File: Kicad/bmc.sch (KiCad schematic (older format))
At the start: 26 parts, among them J1601 Header, J1602 Header, J1603 Conn_01x05, J1605 Double-mini-DIN-6, SW1601 SW_DIP_x01, SW1602 SW_DIP_x01, U1601 STM32F031K6T6

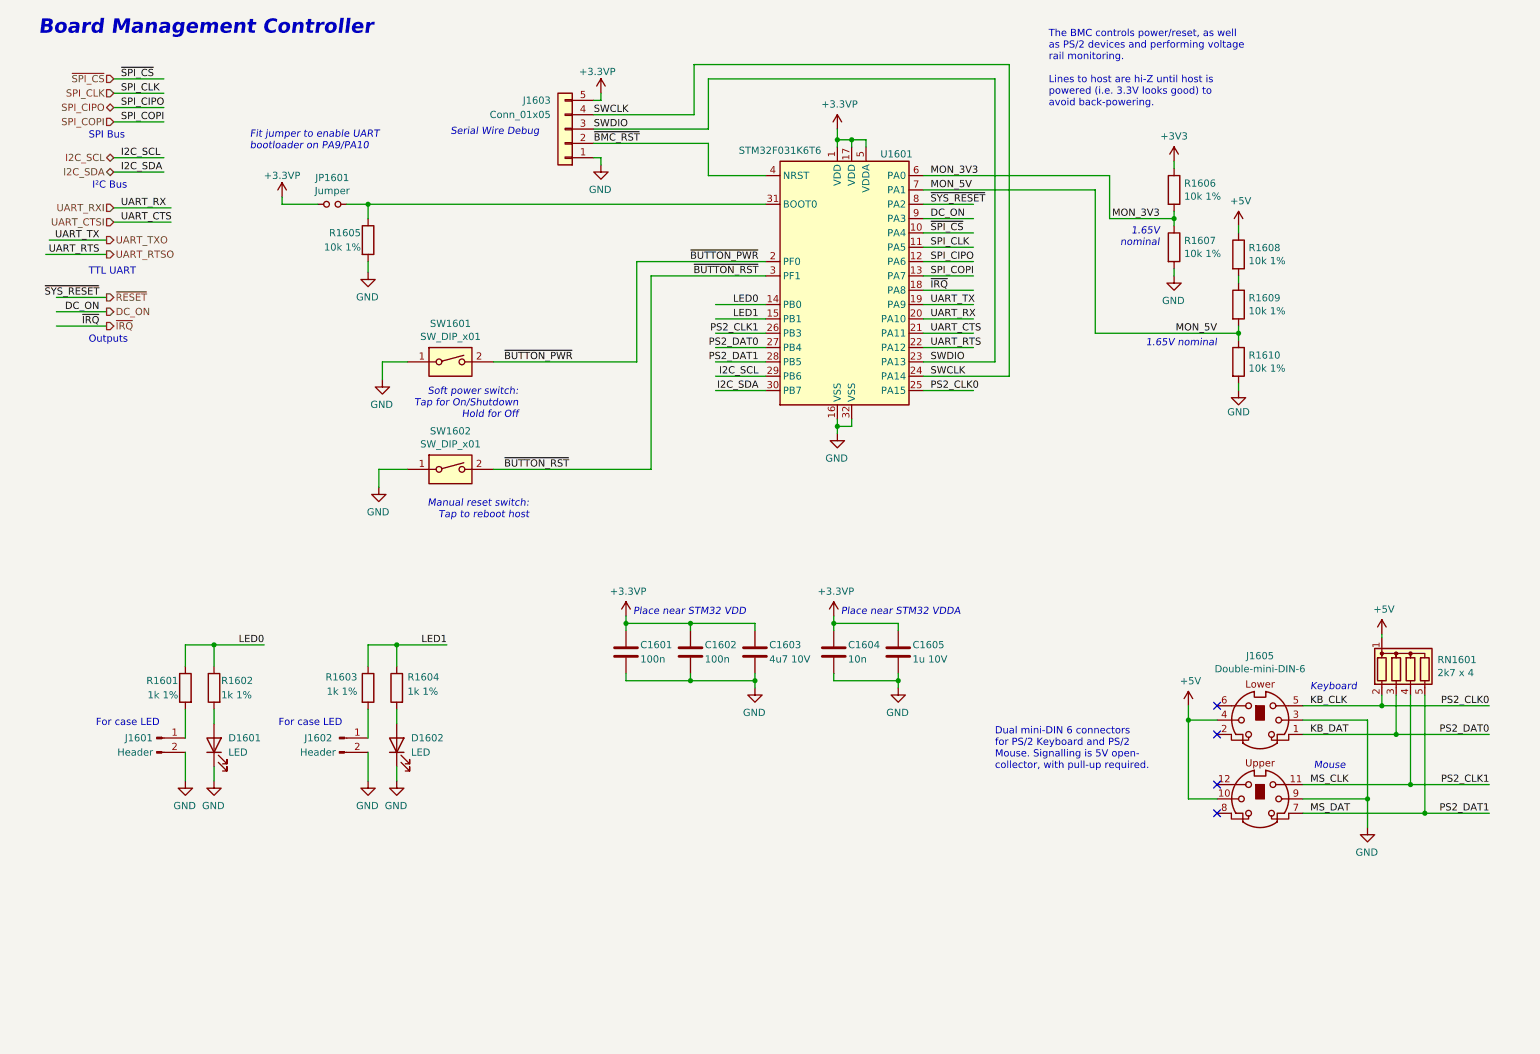
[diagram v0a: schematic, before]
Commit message: Revised PSU switch-on circuit.
Updated notes on BMC and Audio sheet.
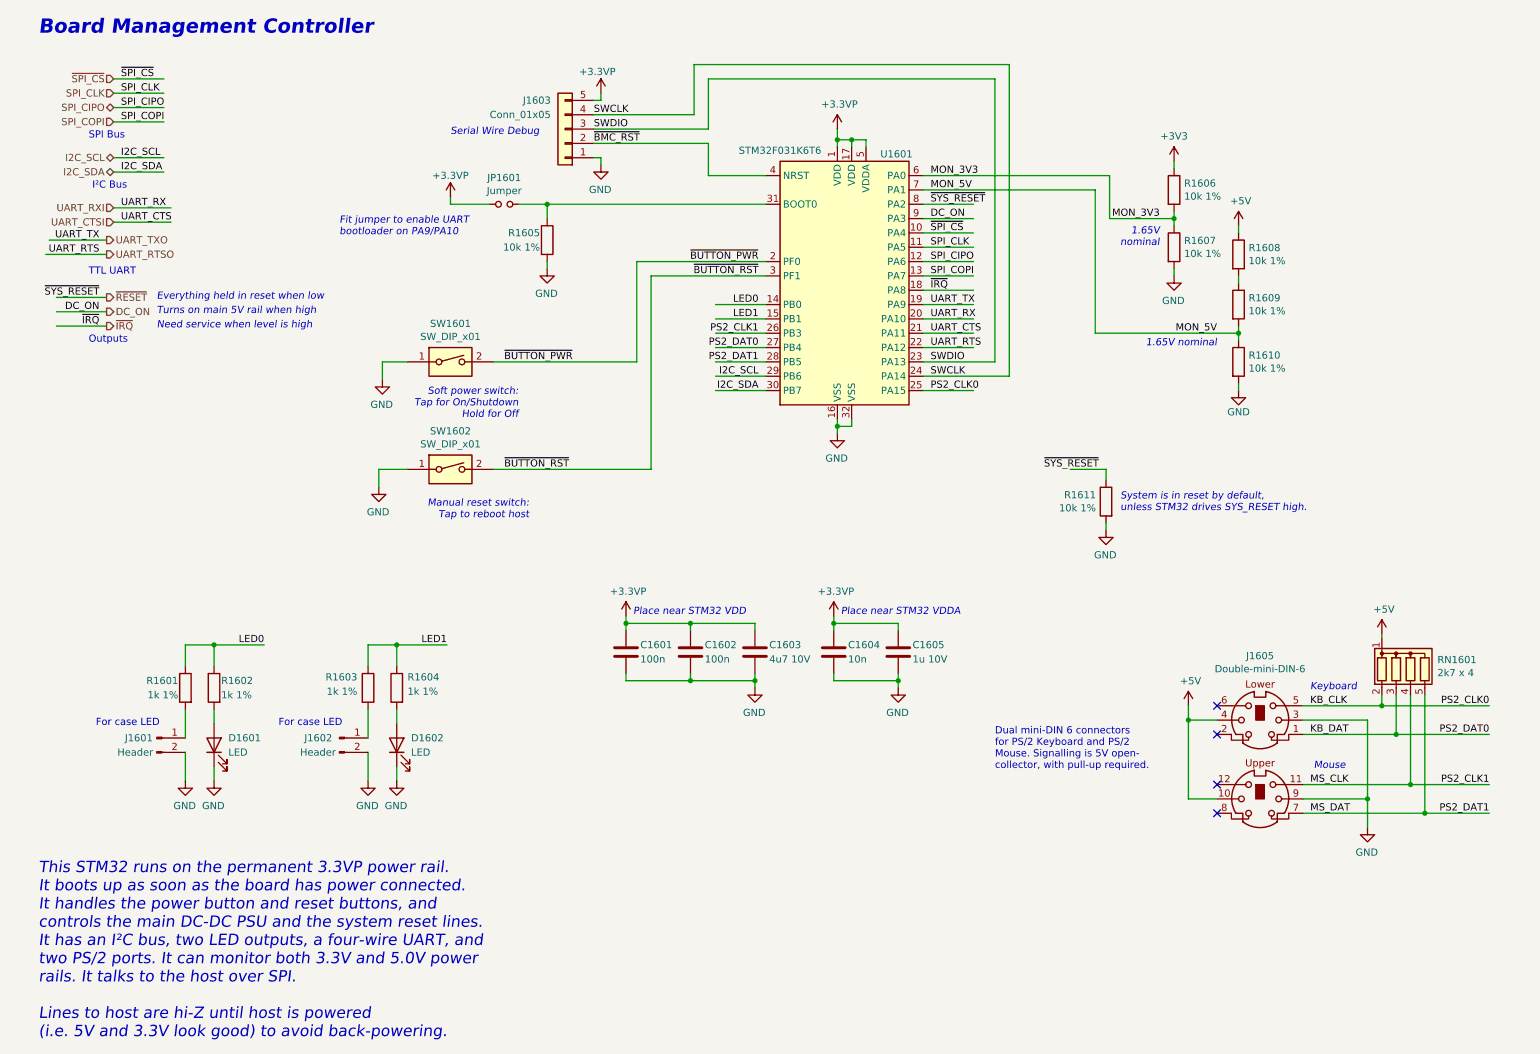
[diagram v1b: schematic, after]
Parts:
- added R1611: 10k 1%, Resistor_SMD:R_0805_2012Metric_Pad1.20x1.40mm_HandSolder, symbol Device:R
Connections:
- wire segments 147 -> 150
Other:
- note added: "Everything held in reset when low"
- note added: "Need service when level is high"
- note added: "System is in reset by default,\nunless STM32 drives SYS_RESET high."
- note added: "This STM32 runs on the permanent 3.3VP power rail.\nIt boots up as soon as the board has power connected.\nIt handles the power button and reset buttons, and\ncontrols the main DC-DC PSU and the system reset lines.\nIt has an I²C bus, two LED outputs, a four-wire UART, and\ntwo PS/2 ports. It can monitor both 3.3V and 5.0V power\nrails. It talks to the host over SPI.\n\nLines to host are hi-Z unt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"
- note added: "Turns on main 5V rail when high"
- note removed: "The BMC controls power/reset, as well\nas PS/2 devices and performing voltage\nrail monitoring.\n\nLines to host are hi-Z until host is\npowered (i.e. 3.3V looks good) to\navoid back-powering."
- moved on the sheet: JP1601, R1605
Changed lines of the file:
@@
 encoding utf-8
 Sheet 16 17
-Title ""
+Title "Neotron Common Hardware - Board M'gmt Controller"
 Date ""
-Rev ""
-Comp ""
-Comment1 ""
-Comment2 ""
+Rev "[Uncontrolled]"
+Comp "https://neotron-compute.github.io/"
+Comment1 "Licenced as CC BY-SA"
+Comment2 "Copyright (c) The Neotron Developers, 2021"
 Comment3 ""
 Comment4 ""
@@
 Text Notes 3975 4075 2    50   Italic 0
 Manual reset switch:\nTap to reboot host
-Text Notes 7600 1200 0    50   ~ 0
-The BMC controls power/reset, as well\nas PS/2 devices and performing voltage\nrail monitoring.\n\nLines to host are hi-Z until host is\npowered (i.e. 3.3V looks good) to\navoid back-powering.
 $Comp
 L Device:C C1603
@@
 L Device:Jumper_NO_Small JP1601
 U 1 1 6072F924
-P 2600 1875
-F 0 "JP1601" H 2600 2060 50  0000 C CNN
-F 1 "Jumper" H 2600 1969 50  0000 C CNN
-F 2 "Connector_PinHeader_2.54mm:PinHeader_1x02_P2.54mm_Vertical" H 2600 1875 50  0001 C CNN
-F 3 "~" H 2600 1875 50  0001 C CNN
-F 4 "1" H 2600 1875 50  0001 C CNN "DNP"
-F 5 "~" H 2600 1875 50  0001 C CNN "Digikey"
-F 6 "~" H 2600 1875 50  0001 C CNN "MPN"
-F 7 "~" H 2600 1875 50  0001 C CNN "Manufacturer"
-	1    2600 1875
+P 3800 1875
+F 0 "JP1601" H 3800 2060 50  0000 C CNN
+F 1 "Jumper" H 3800 1969 50  0000 C CNN
+F 2 "Connector_PinHeader_2.54mm:PinHeader_1x02_P2.54mm_Vertical" H 3800 1875 50  0001 C CNN
+F 3 "~" H 3800 1875 50  0001 C CNN
+F 4 "1" H 3800 1875 50  0001 C CNN "DNP"
+F 5 "~" H 3800 1875 50  0001 C CNN "Digikey"
+F 6 "~" H 3800 1875 50  0001 C CNN "MPN"
+F 7 "~" H 3800 1875 50  0001 C CNN "Manufacturer"
+	1    3800 1875
 	1    0    0    -1
 $EndComp
@@
 L power:+3.3VP #PWR01607
 U 1 1 606E2A06
-P 2250 1825
-F 0 "#PWR01607" H 2400 1775 50  0001 C CNN
-F 1 "+3.3VP" H 2250 1975 50  0000 C CNN
-F 2 "" H 2250 1825 50  0001 C CNN
-F 3 "" H 2250 1825 50  0001 C CNN
-	1    2250 1825
+P 3425 1825
+F 0 "#PWR01607" H 3575 1775 50  0001 C CNN
+F 1 "+3.3VP" H 3425 1975 50  0000 C CNN
+F 2 "" H 3425 1825 50  0001 C CNN
+F 3 "" H 3425 1825 50  0001 C CNN
+	1    3425 1825
 	1    0    0    -1
 $EndComp
@@
 	6325 1425 6325 1475
 Wire Wire Line
-	2250 1825 2250 1875
+	3425 1825 3425 1875
 Wire Wire Line
 	5625 2575 5275 2575
@@
 Serial Wire Debug
 Wire Wire Line
-	2700 1875 2850 1875
+	3900 1875 4100 1875
 Wire Wire Line
 	6725 2975 7225 2975
@@
 MON_3V3
 Wire Wire Line
-	2250 1875 2500 1875
+	3425 1875 3700 1875
 Wire Wire Line
 	9925 5375 10675 5375
@@
 Wire Wire Line
 	6725 2675 7075 2675
-Text Notes 2025 1500 0    50   Italic 0
+Text Notes 2650 2100 0    50   Italic 0
 Fit jumper to enable UART\nbootloader on PA9/PA10
 Wire Wire Line
@@
 L Device:R R1605
 U 1 1 606E29F2
-P 2850 2125
-F 0 "R1605" H 2800 2175 50  0000 R CNN
-F 1 "10k 1%" H 2800 2075 50  0000 R CNN
-F 2 "Resistor_SMD:R_0805_2012Metric_Pad1.20x1.40mm_HandSolder" V 2780 2125 50  0001 C CNN
-F 3 "~" H 2850 2125 50  0001 C CNN
-F 4 "0" H 2850 2125 50  0001 C CNN "DNP"
-F 5 "RMCF0805FT10K0-ND" H 2850 2125 50  0001 C CNN "Digikey"
-F 6 "RMCF0805FT10K0" H 2850 2125 50  0001 C CNN "MPN"
-F 7 "Stackpole" H 2850 2125 50  0001 C CNN "Manufacturer"
-	1    2850 2125
+P 4100 2125
+F 0 "R1605" H 4050 2175 50  0000 R CNN
+F 1 "10k 1%" H 4050 2075 50  0000 R CNN
+F 2 "Resistor_SMD:R_0805_2012Metric_Pad1.20x1.40mm_HandSolder" V 4030 2125 50  0001 C CNN
+F 3 "~" H 4100 2125 50  0001 C CNN
+F 4 "0" H 4100 2125 50  0001 C CNN "DNP"
+F 5 "RMCF0805FT10K0-ND" H 4100 2125 50  0001 C CNN "Digikey"
+F 6 "RMCF0805FT10K0" H 4100 2125 50  0001 C CNN "MPN"
+F 7 "Stackpole" H 4100 2125 50  0001 C CNN "Manufacturer"
+	1    4100 2125
 	1    0    0    -1
 $EndComp
@@
 	4825 2375 4825 3725
 Wire Wire Line
-	6725 1875 7075 1875
-Wire Wire Line
 	6725 1975 7075 1975
 Text Notes 900  1425 0    50   ~ 0
@@
 	7225 1000 7225 2975
 Wire Wire Line
-	2850 1875 5625 1875
-Connection ~ 2850 1875
-Wire Wire Line
-	2850 1875 2850 1975
+	4100 1875 5625 1875
+Connection ~ 4100 1875
+Wire Wire Line
+	4100 1875 4100 1975
 $Comp
 L power:GND #PWR0133
 U 1 1 6086D93C
-P 2850 2350
-F 0 "#PWR0133" H 2850 2100 50  0001 C CNN
-F 1 "GND" H 2855 2177 50  0000 C CNN
-F 2 "" H 2850 2350 50  0001 C CNN
-F 3 "" H 2850 2350 50  0001 C CNN
-	1    2850 2350
-	-1   0    0    -1
-$EndComp
-Wire Wire Line
-	2850 2350 2850 2275
+P 4100 2325
+F 0 "#PWR0133" H 4100 2075 50  0001 C CNN
+F 1 "GND" H 4105 2152 50  0000 C CNN
+F 2 "" H 4100 2325 50  0001 C CNN
+F 3 "" H 4100 2325 50  0001 C CNN
+	1    4100 2325
+	-1   0    0    -1
+$EndComp
+Wire Wire Line
+	4100 2325 4100 2275
 Text Notes 900  2375 0    50   ~ 0
 TTL UART
@@
 Wire Wire Line
 	1025 2625 675  2625
-Text HLabel 1025 2625 2    50   Output ~ 0
-DC_ON
 Text Label 975  2525 2    50   ~ 0
 ~SYS_RESET
@@
 Wire Wire Line
 	1025 2225 600  2225
+$Comp
+L Device:R R1611
+U 1 1 6071F9F2
+P 8000 3950
+F 0 "R1611" H 8070 3996 50  0000 L CNN
+F 1 "10k 1%" H 8070 3905 50  0000 L CNN
+F 2 "Resistor_SMD:R_0805_2012Metric_Pad1.20x1.40mm_HandSolder" V 7930 3950 50  0001 C CNN
+F 3 "~" H 8000 3950 50  0001 C CNN
+F 4 "0" H 8000 3950 50  0001 C CNN "DNP"
+F 5 "RMCF0805FT10K0-ND" H 8000 3950 50  0001 C CNN "Digikey"
+F 6 "RMCF0805FT10K0" H 8000 3950 50  0001 C CNN "MPN"
+F 7 "Stackpole" H 8000 3950 50  0001 C CNN "Manufacturer"
+	1    8000 3950
+	-1   0    0    -1
+$EndComp
+Wire Wire Line
+	8000 3725 8000 3800
+Wire Wire Line
+	8000 4100 8000 4150
+$Comp
+L power:GND #PWR01610
+U 1 1 607270B5
+P 8000 4150
+F 0 "#PWR01610" H 8000 3900 50  0001 C CNN
+F 1 "GND" H 8005 3977 50  0000 C CNN
+F 2 "" H 8000 4150 50  0001 C CNN
+F 3 "" H 8000 4150 50  0001 C CNN
+	1    8000 4150
+	-1   0    0    -1
+$EndComp
+Wire Wire Line
+	6725 1875 7075 1875
+Text Label 7950 3725 2    50   ~ 0
+~SYS_RESET
+Wire Wire Line
+	7750 3725 8000 3725
+Text Notes 8100 4025 0    50   Italic 0
+System is in reset by default,\nunless STM32 drives SYS_RESET high.
+Text Notes 1375 2550 0    50   Italic 0
+Everything held in reset when low
+Text Notes 1375 2650 0    50   Italic 0
+Turns on main 5V rail when high
+Text HLabel 1025 2625 2    50   Output ~ 0
+DC_ON
+Text Notes 1375 2750 0    50   Italic 0
+Need service when level is high
+Text Notes 550  7700 0    79   Italic 0
+This STM32 runs on the permanent 3.3VP power rail.\nIt boots up as soon as the board has power connected.\nIt handles the power button and reset buttons, and\ncontrols the main DC-DC PSU and the system reset lines.\nIt has an I²C bus, two LED outputs, a four-wire UART, and\ntwo PS/2 ports. It can monitor both 3.3V and 5.0V power\nrails. It talks to the host over SPI.\n\nLines to host are hi-Z until host is powered\n(i.e. 5V and 3.3V look good) to avoid back-powering.
 $EndSCHEMATC

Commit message: Brought in sheets from Neotron Pico.
Also includes DB15HD and PSU 3D models.
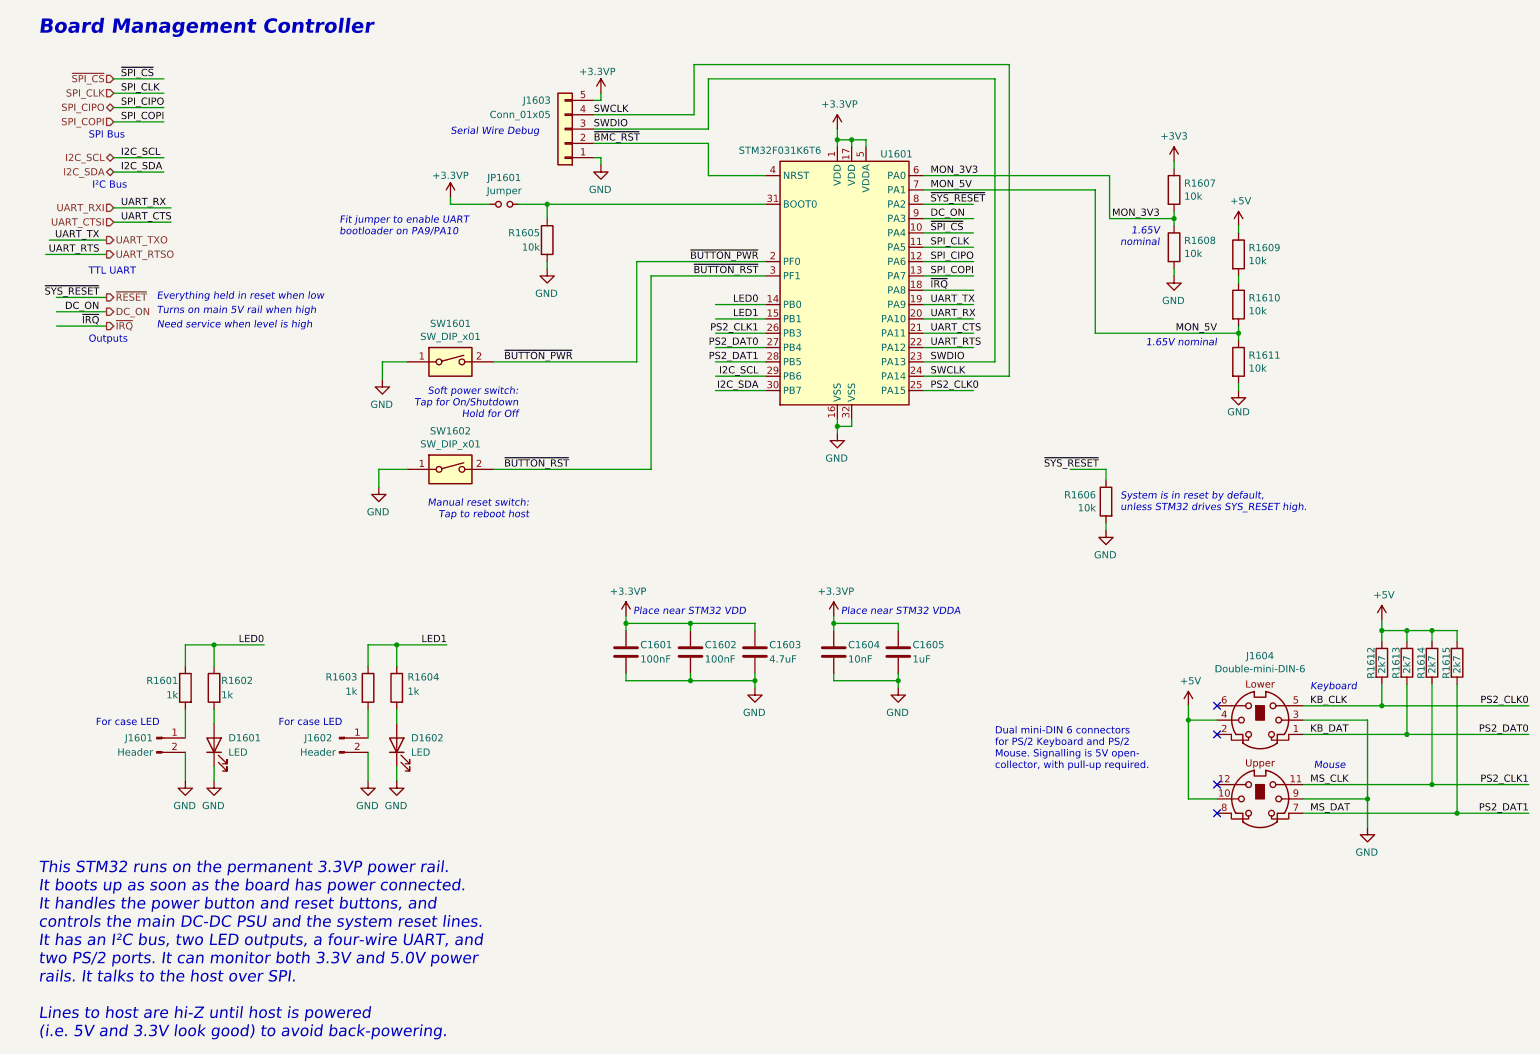
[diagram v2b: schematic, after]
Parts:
- removed RN1601: 2k7 x 4, Resistor_THT:R_Array_SIP5, symbol Device:R_Network04
- added R1612, R1613, R1614, R1615: 2k7, Resistor_SMD:R_0805_2012Metric_Pad1.20x1.40mm_HandSolder, symbol Device:R
- C1601, C1602: value 100n -> 100nF; Digikey BC1150CT-ND -> (none); LCSC Part# (none) -> C49678; MPN K104K15X7RF5TL2 -> CPL-CAP-X7R-0805-100NF-50V; Manufacturer Vishay -> CPL; Mouser 594-K104K15X7RF5TL2 -> (none)
- C1603: value 4u7 10V -> 4.7uF; Digikey 1276-6464-1-ND -> (none); LCSC Part# (none) -> C1779; MPN CL21A475KPFNNNG -> CPL-CAP-X5R-0805-4.7UF-25V; Manufacturer Samsung -> CPL
- C1604: value 10n -> 10nF; LCSC Part# (none) -> C1710
- C1605: value 1u 10V -> 1uF; Digikey 1276-6471-1-ND -> (none); LCSC Part# (none) -> C28323; MPN CL21B105KOFNNNG -> CPL-CAP-X7R-0805-1UF-25V; Manufacturer Samsung -> CPL
- D1601, D1602: MPN 151031SS06000 -> CPL-LED-3MM-RED; Manufacturer Würth -> CPL
- R1601, R1602, R1603, R1604: value 1k 1% -> 1k; Digikey RMCF0805FT1K00-ND -> (none); LCSC Part# (none) -> C17513; MPN RMCF0805FT1K00 -> CPL-RES-0805-1K-0.125W; Manufacturer Stackpole -> CPL
- R1605: value 10k 1% -> 10k; Digikey RMCF0805FT10K0-ND -> (none); LCSC Part# (none) -> C17414; MPN RMCF0805FT10K0 -> CPL-RES-0805-10K-0.125W; Manufacturer Stackpole -> CPL
- R1606: renamed from R1611; value 10k 1% -> 10k; Digikey RMCF0805FT10K0-ND -> (none); LCSC Part# (none) -> C17414; MPN RMCF0805FT10K0 -> CPL-RES-0805-10K-0.125W; Manufacturer Stackpole -> CPL
- R1607: renamed from R1606; value 10k 1% -> 10k; Digikey RMCF0805FT10K0-ND -> (none); LCSC Part# (none) -> C17414; MPN RMCF0805FT10K0 -> CPL-RES-0805-10K-0.125W; Manufacturer Stackpole -> CPL
- R1608: renamed from R1607; value 10k 1% -> 10k; Digikey RMCF0805FT10K0-ND -> (none); LCSC Part# (none) -> C17414; MPN RMCF0805FT10K0 -> CPL-RES-0805-10K-0.125W; Manufacturer Stackpole -> CPL
- R1609: renamed from R1608; value 10k 1% -> 10k; Digikey RMCF0805FT10K0-ND -> (none); LCSC Part# (none) -> C17414; MPN RMCF0805FT10K0 -> CPL-RES-0805-10K-0.125W; Manufacturer Stackpole -> CPL
- R1610: renamed from R1609; value 10k 1% -> 10k; Digikey RMCF0805FT10K0-ND -> (none); LCSC Part# (none) -> C17414; MPN RMCF0805FT10K0 -> CPL-RES-0805-10K-0.125W; Manufacturer Stackpole -> CPL
- R1611: renamed from R1610; value 10k 1% -> 10k; Digikey RMCF0805FT10K0-ND -> (none); LCSC Part# (none) -> C17414; MPN RMCF0805FT10K0 -> CPL-RES-0805-10K-0.125W; Manufacturer Stackpole -> CPL
- U1601: LCSC Part# (none) -> C526904
- renumbered J1605 to J1604
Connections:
- wire segments 150 -> 157

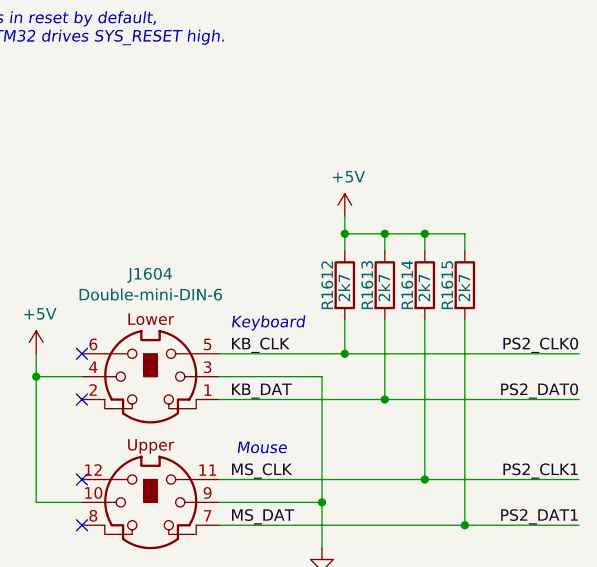
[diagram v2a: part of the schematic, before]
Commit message: Merge in more changes.
Mostly lowering voltage tolerances to minimum required.
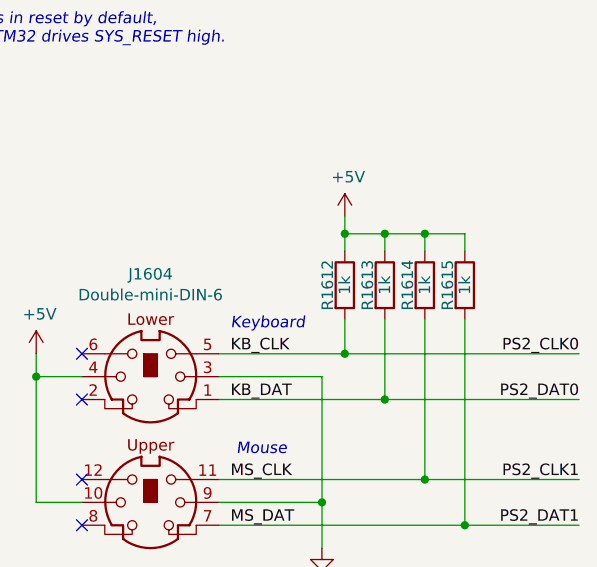
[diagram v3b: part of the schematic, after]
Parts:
- C1601, C1602, C1603, C1604, C1605: Tolerance (none) -> X5R; Voltage (none) -> 10V
- D1601, D1602: Digikey 732-5006-ND -> (none); Mouser 151031SS06000 -> (none)
- R1601, R1602, R1603, R1604, R1605, R1606, R1607, R1608, R1609, R1610, R1611: Tolerance (none) -> 1%
- R1612, R1613, R1614, R1615: value 2k7 -> 1k; DNP (none) -> 0; LCSC Part# (none) -> C17513; MPN (none) -> CPL-RES-0805-1K-0.125W; Manufacturer (none) -> CPL; Tolerance (none) -> 1%
